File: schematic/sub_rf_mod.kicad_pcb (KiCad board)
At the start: 2 copper layers, 69.1 x 50 mm, 36 parts, among them J4B1 Conn_01x08

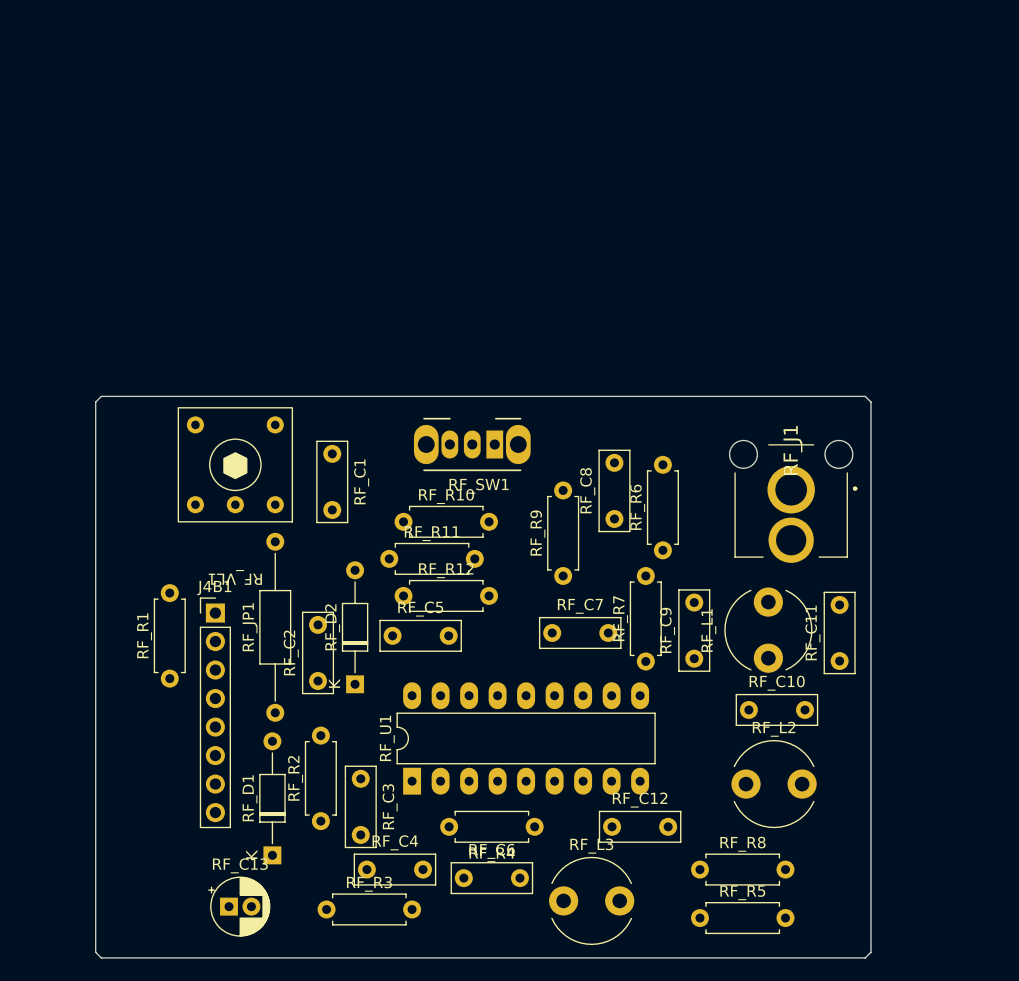
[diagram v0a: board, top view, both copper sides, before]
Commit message: imporved power rails, added 3D models (primitives at this point till others can be made).
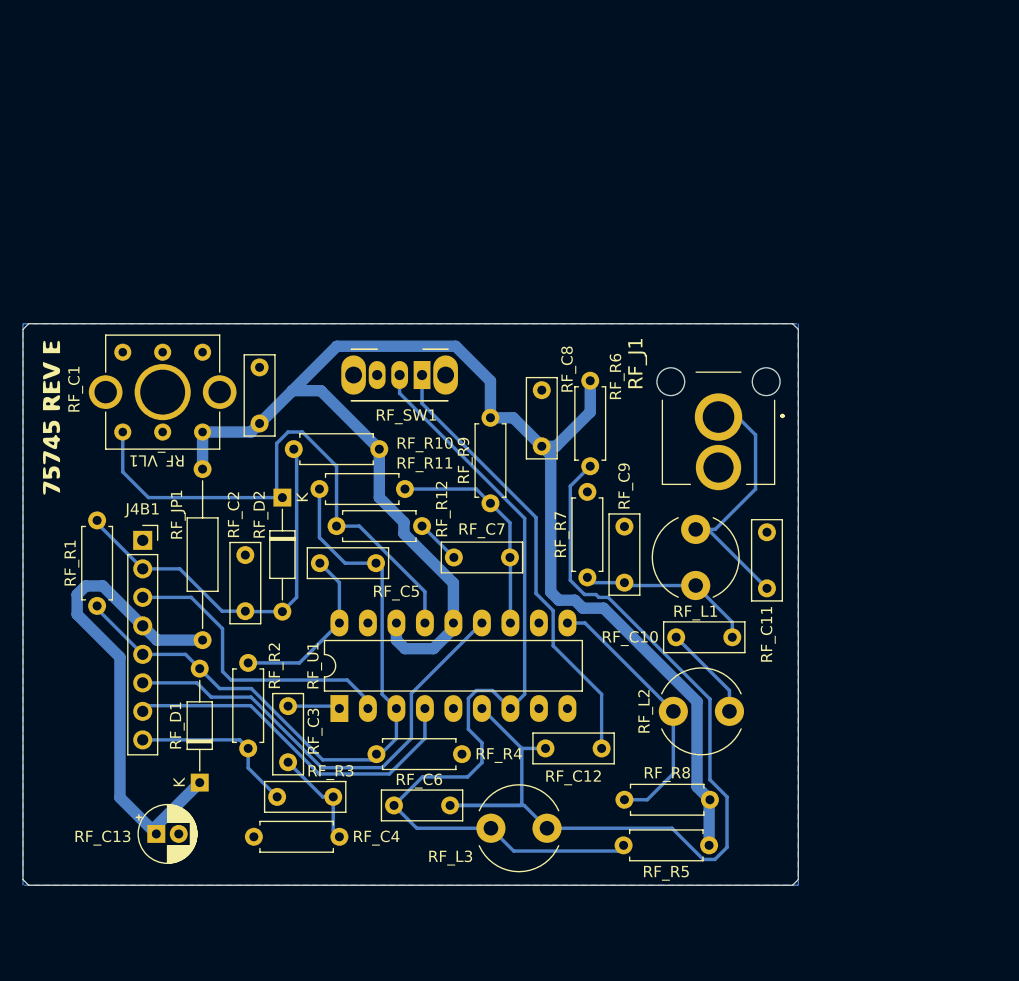
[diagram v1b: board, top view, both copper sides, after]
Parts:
- added S5: rf_board_rev, logos:rf_board_revision, F.Cu at (103.3, 81.7)
- J4B1: footprint Connector_PinHeader_2.54mm:PinHeader_1x08_P2.54mm_Vertical -> Connector_PinSocket_2.54mm:PinSocket_1x08_P2.54mm_Vertical
- RF_J1: footprint RCJ-041:RCJ041 -> RCJ-041:RCJ041_copy
- moved RF_JP1 22.7 mm to (116.7, 86.2), turned to -90 degrees
- moved RF_D2 17.9 mm to (123.8, 88.8), turned to -90 degrees
- moved RF_R2 15.5 mm to (120.8, 103.5), turned to -90 degrees
- moved RF_C2 13.0 mm to (120.5, 93.9), turned to -90 degrees
- moved RF_C7 11.0 mm to (139.1, 94.1)
- moved RF_R6 9.90 mm to (151.3, 86.0)
- moved RF_C9 9.20 mm to (154.3, 96.4)
- moved RF_R8 9.17 mm to (154.3, 115.7)
- moved RF_C10 9.16 mm to (158.9, 101.2)
- moved RF_C5 9.16 mm to (127.2, 94.6)
- moved RF_C8 9.16 mm to (146.9, 84.2)
- moved RF_D1 9.16 mm to (116.5, 114.2)
- moved RF_L1 9.16 mm to (160.7, 96.6)
- moved RF_R1 9.16 mm to (107.3, 98.4)
- moved RF_R3 9.16 mm to (121.3, 119.0)
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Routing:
- net (no net): track 0.00 -> 764.1 mm
- added copper zone on B.Cu, net (none)

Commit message: fixed cart for 12 mil isolation routing. Now minimum trace isolation is 12 mil. Trace width min is 12 mil. This is easier to build.
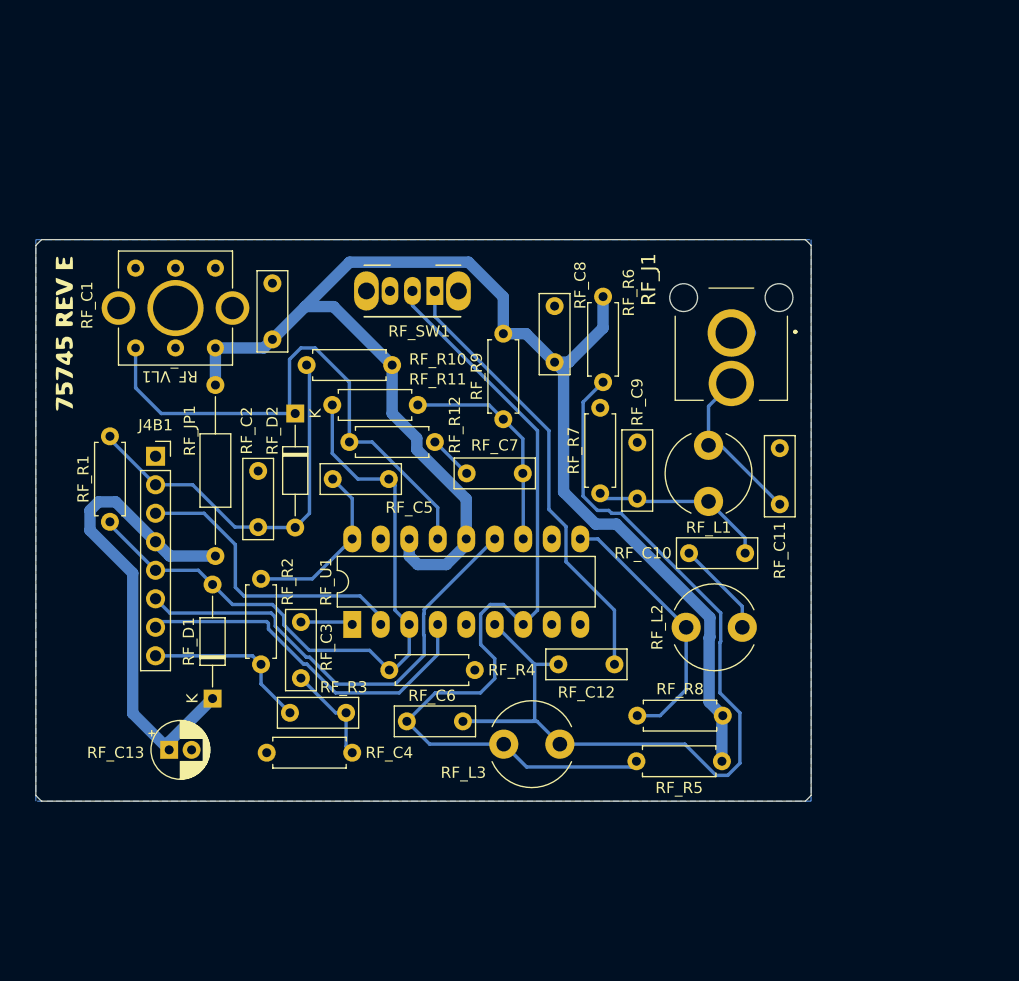
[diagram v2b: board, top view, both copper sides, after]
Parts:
- moved RF_C11 7.58 mm to (168.1, 89.4)
- moved RF_C13 7.58 mm to (113.7, 111.3)
- moved RF_C3 7.58 mm to (125.5, 99.9)
- moved RF_JP1 7.58 mm to (117.9, 78.7)
- moved RF_R12 7.58 mm to (137.4, 83.8)
- moved RF_R7 7.58 mm to (152.1, 88.4)
- moved RF_R8 7.58 mm to (155.4, 108.2)
- moved RF_R9 7.58 mm to (143.5, 81.8)
- moved RF_U1 7.58 mm to (130.0, 100.1)
- moved J4B1 7.58 mm to (112.5, 85.1)
- moved RF_C1 7.58 mm to (122.9, 74.7)
- moved RF_C10 7.58 mm to (160.1, 93.7)
- moved RF_C12 7.58 mm to (153.4, 103.6)
- moved RF_C2 7.58 mm to (121.7, 86.4)
- moved RF_C4 7.58 mm to (129.5, 108.0)
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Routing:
- net (no net): track 764.1 -> 757.2 mm

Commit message: update 3d image and pcbs for export
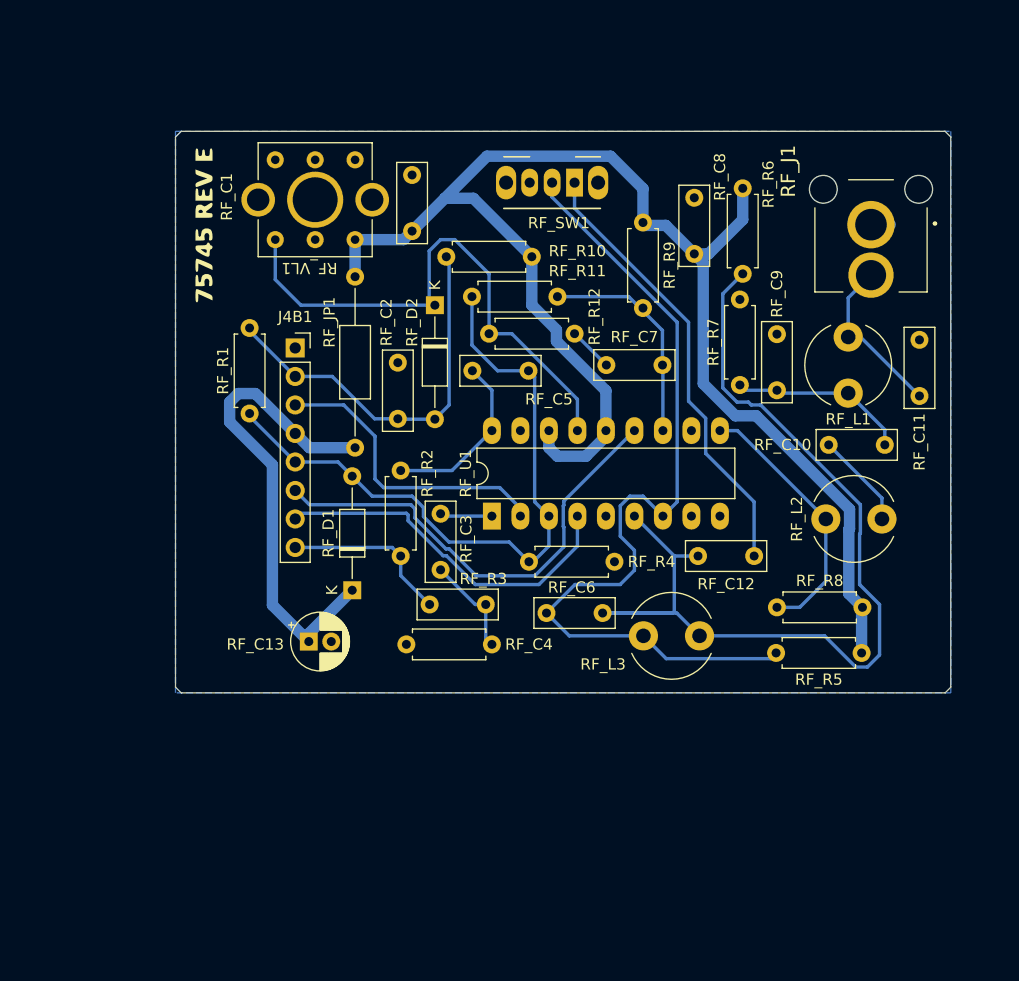
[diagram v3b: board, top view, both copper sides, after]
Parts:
- RF_SW1: footprint Button_Switch_THT:SW_CuK_OS102011MA1QN1_SPDT_Angled -> Switches_THT:SW_CuK_OS102011MA1QN1_SPDT_Angled
- moved RF_R9 21.5 mm to (156.0, 64.3), turned to -90 degrees
- moved RF_C6 15.8 mm to (147.4, 99.1)
- moved RF_R7 15.8 mm to (164.6, 78.7)
- moved RF_SW1 15.8 mm to (149.9, 60.7)
- moved RF_R12 15.8 mm to (149.9, 74.2)
- moved RF_R2 15.8 mm to (134.4, 86.4)
- moved RF_VL1 15.8 mm to (126.7, 62.2)
- moved J4B1 15.8 mm to (125.0, 75.4)
- moved RF_C1 15.8 mm to (135.4, 65.0)
- moved RF_C10 15.8 mm to (172.5, 84.1)
- moved RF_C11 15.8 mm to (180.6, 79.7)
- moved RF_C12 15.8 mm to (165.9, 94.0)
- moved RF_C13 15.8 mm to (126.2, 101.6)
- moved RF_C2 15.8 mm to (134.1, 76.7)
- moved RF_C3 15.8 mm to (137.9, 90.2)
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
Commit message: cleanup and readjust of traces, copied to gerber export projects.
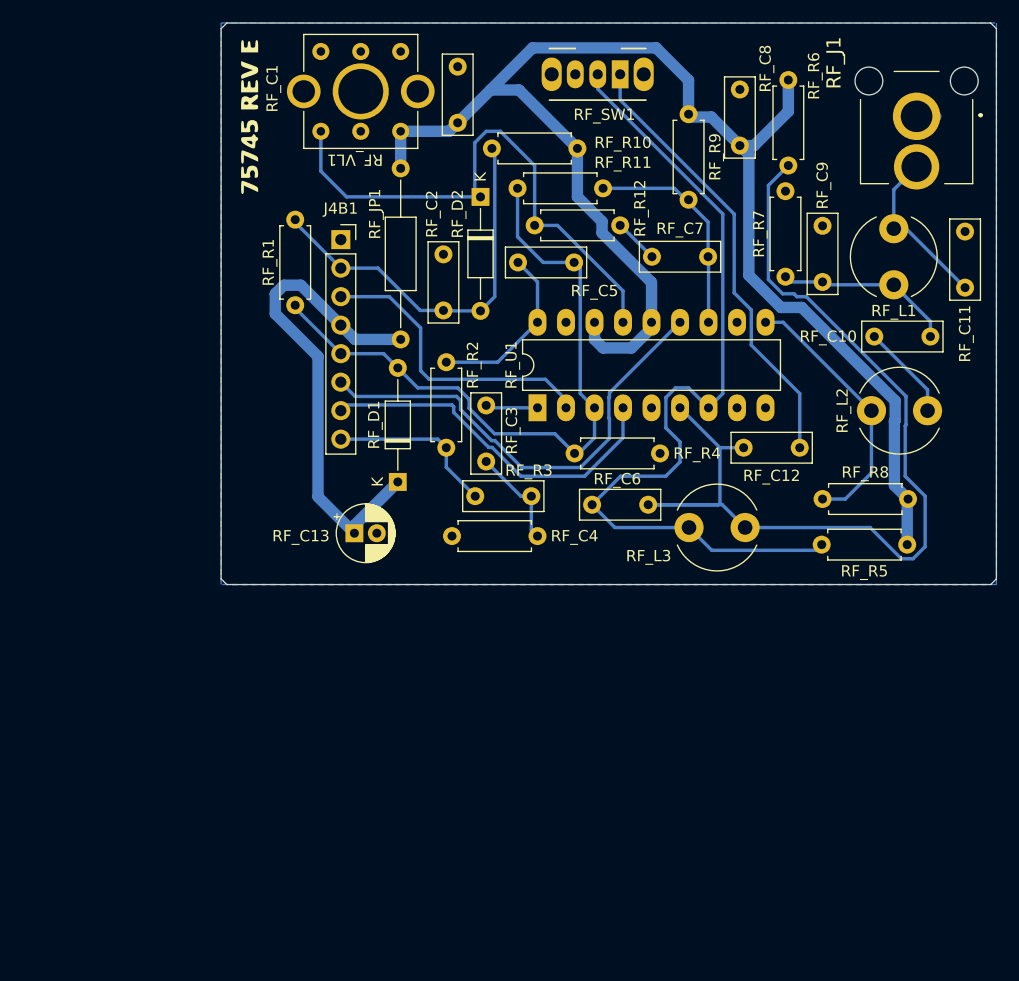
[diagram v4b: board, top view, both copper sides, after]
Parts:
- moved RF_C7 10.5 mm to (156.8, 67.3)
- moved RF_D2 10.5 mm to (141.5, 62.0)
- moved RF_R5 10.5 mm to (179.5, 93.0)
- moved RF_R9 10.5 mm to (160.0, 54.6)
- moved RF_J1 10.5 mm to (180.3, 54.8)
- moved S5 10.5 mm to (120.9, 54.9)
- moved J4B1 10.5 mm to (129.0, 65.8)
- moved RF_C8 10.5 mm to (164.6, 57.4)
- moved RF_JP1 10.5 mm to (134.4, 59.4)
- moved RF_R1 10.5 mm to (125.0, 71.6)
- moved RF_C1 10.5 mm to (139.4, 55.4)
- moved RF_C10 10.5 mm to (176.6, 74.4)
- moved RF_C11 10.5 mm to (184.7, 70.1)
- moved RF_C12 10.5 mm to (169.9, 84.3)
- moved RF_C13 10.5 mm to (130.2, 91.9)
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
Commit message: added mounting holes, future proof the video section for jumper selection of voltages between 4516/4116 chips
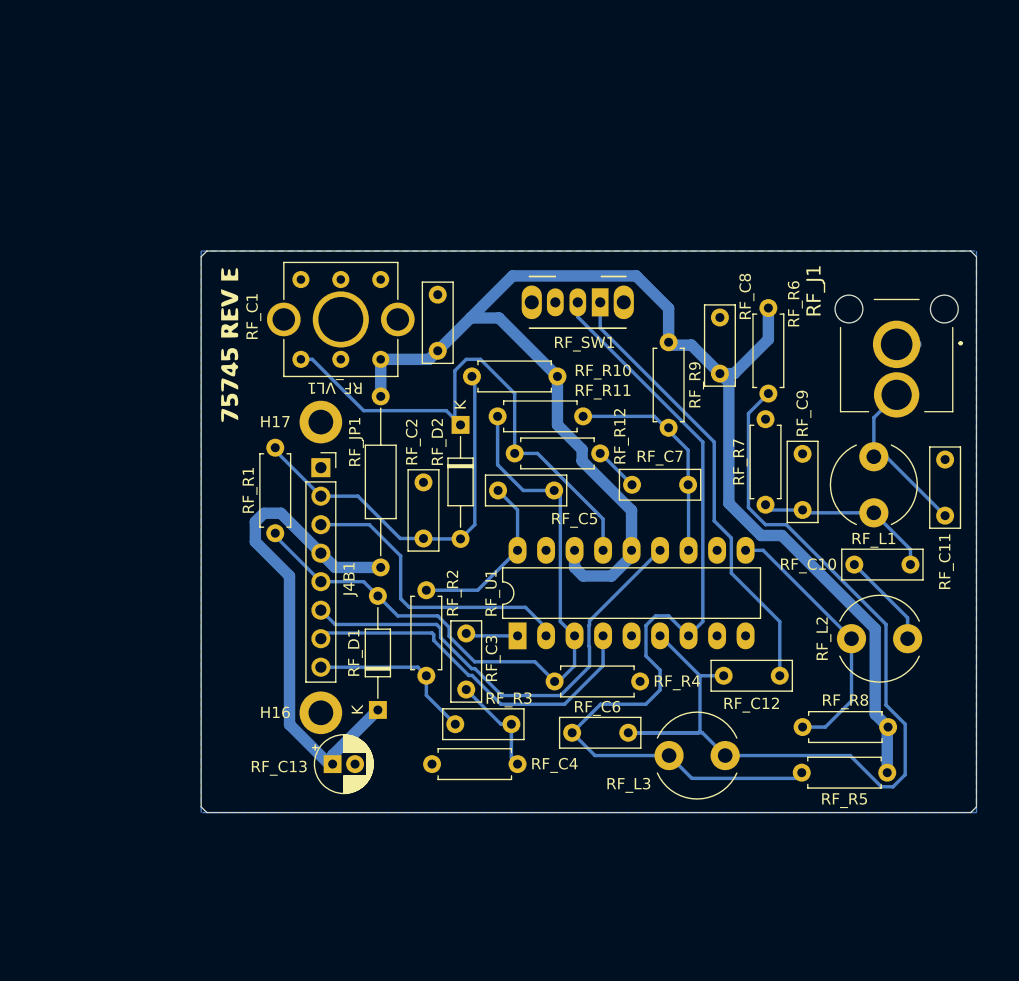
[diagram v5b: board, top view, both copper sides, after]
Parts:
- added H16: MountingHole_Pad, MountingHole:MountingHole_2.2mm_M2_DIN965_Pad, F.Cu at (127.3, 108.0)
- added H17: MountingHole_Pad, MountingHole:MountingHole_2.2mm_M2_DIN965_Pad, F.Cu at (127.3, 82.0)
- moved RF_C13 20.7 mm to (128.3, 112.5)
- moved RF_C10 20.4 mm to (174.8, 94.7)
- moved RF_C11 20.4 mm to (182.9, 90.4)
- moved RF_C5 20.4 mm to (143.0, 88.1)
- moved RF_C9 20.4 mm to (170.2, 89.9)
- moved RF_D2 20.4 mm to (139.7, 82.3)
- moved RF_L2 20.4 mm to (174.5, 101.3)
- moved RF_L3 20.4 mm to (158.3, 111.8)
- moved RF_R11 20.4 mm to (143.0, 81.5)
- moved RF_R2 20.4 mm to (136.7, 97.0)
- moved RF_R3 20.4 mm to (137.2, 112.5)
- moved RF_R4 20.4 mm to (155.7, 105.2)
- moved RF_R5 20.4 mm to (177.7, 113.3)
- moved RF_R7 20.4 mm to (166.9, 89.4)
- moved RF_R9 20.4 mm to (158.2, 74.9)
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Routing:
- net (no net): track 757.0 -> 755.5 mm

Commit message: updated schematic PDF, updated 3D image. Updated all gerber files, and small adjustments to the pcb to cleanup traces.
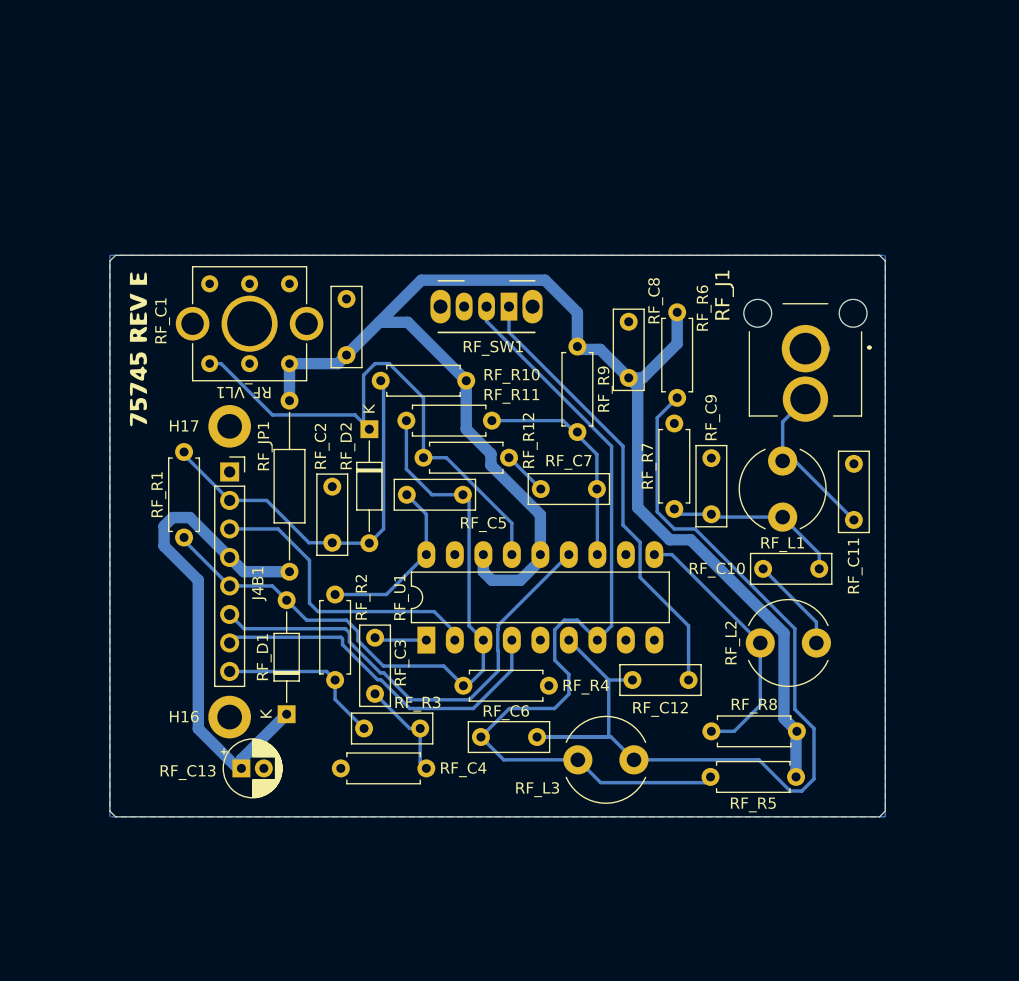
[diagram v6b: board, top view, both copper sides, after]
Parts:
- moved RF_C1 8.14 mm to (129.5, 76.1)
- moved RF_C10 8.14 mm to (166.7, 95.1)
- moved RF_C13 8.14 mm to (120.2, 112.9)
- moved RF_C5 8.14 mm to (134.9, 88.5)
- moved RF_C9 8.14 mm to (162.1, 90.3)
- moved RF_J1 8.14 mm to (170.4, 75.5)
- moved RF_L1 8.14 mm to (168.4, 90.5)
- moved RF_L2 8.14 mm to (166.4, 101.7)
- moved RF_L3 8.14 mm to (150.2, 112.1)
- moved RF_R10 8.14 mm to (140.2, 78.4)
- moved RF_R11 8.14 mm to (134.9, 81.9)
- moved RF_R6 8.14 mm to (159.0, 79.9)
- moved RF_R8 8.14 mm to (162.1, 109.6)
- moved RF_U1 8.14 mm to (136.7, 101.5)
- moved RF_VL1 8.14 mm to (120.9, 73.3)
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
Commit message: fixed cap value, adjusted rf lines on main board to make npt hole assembly easier
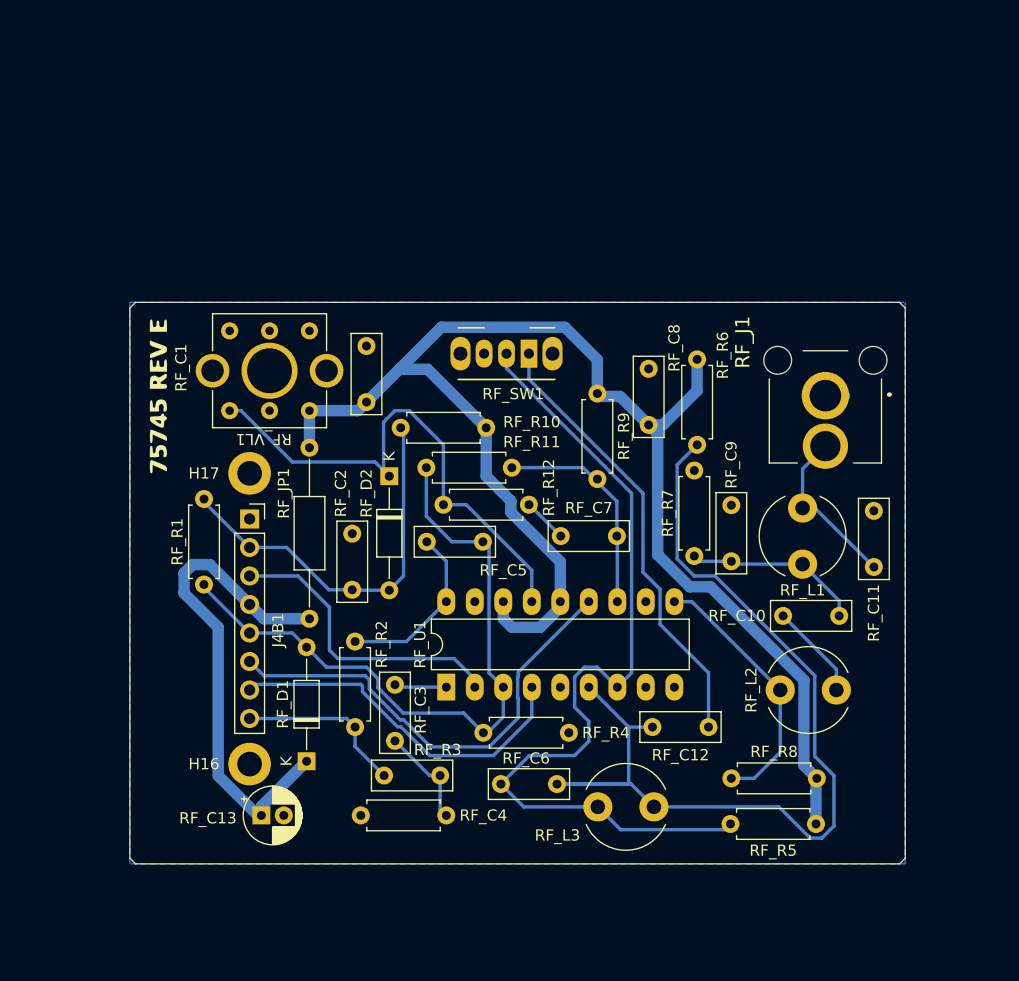
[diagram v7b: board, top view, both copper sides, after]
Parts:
- RF_C2: value 10pF -> 10nF
- moved RF_C1 4.55 mm to (131.3, 80.3)
- moved RF_L1 4.55 mm to (170.2, 94.7)
- moved RF_R6 4.55 mm to (160.8, 84.1)
- moved RF_R8 4.55 mm to (163.8, 113.8)
- moved RF_U1 4.55 mm to (138.4, 105.7)
- moved RF_JP1 4.55 mm to (126.2, 84.3)
- moved RF_R1 4.55 mm to (116.8, 96.5)
- moved RF_VL1 4.55 mm to (122.7, 77.5)
- moved H16 4.55 mm to (120.9, 112.5)
- moved H17 4.55 mm to (120.9, 86.6)
- moved J4B1 4.55 mm to (120.9, 90.7)
- moved RF_C11 4.55 mm to (176.5, 95.0)
- moved RF_C12 4.55 mm to (161.8, 109.2)
- moved RF_C2 4.55 mm to (130.0, 92.0)
- moved RF_C3 4.55 mm to (133.9, 105.5)
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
